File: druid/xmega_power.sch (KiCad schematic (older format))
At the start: 13 parts, among them P8 CONN_01X02, P9 CONN_01X02, U4 XC6206P332MR

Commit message: Design and connect GSM module.
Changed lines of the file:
@@
 Text HLabel 6875 5250 2    60   Output ~ 0
 3.7V
-Text HLabel 5500 4025 0    60   Output ~ 0
-GND
 Connection ~ 5650 4025
 Connection ~ 4500 2250
@@
 	4700 5600 4700 5875
 Connection ~ 4700 5875
+Text GLabel 5500 4025 0    60   Input ~ 0
+GND
 $EndSCHEMATC

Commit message: + new kbd, but not completed + SRAM lines(labels) replaced by bus
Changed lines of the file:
@@
 LIBS:xmega128a1u_bga100
 LIBS:sim-holders
+LIBS:max7370
 LIBS:xmobile-cache
 EELAYER 25 0
@@
 $Descr A4 11693 8268
 encoding utf-8
-Sheet 4 5
+Sheet 3 5
 Title ""
 Date ""
@@
 	1    0    0    -1
 $EndComp
-Text HLabel 8050 2250 2    60   Output ~ 0
-3.3V
-Text HLabel 6875 5250 2    60   Output ~ 0
-3.7V
 Connection ~ 5650 4025
 Connection ~ 4500 2250
@@
 Text GLabel 5500 4025 0    60   Input ~ 0
 GND
+Text GLabel 8050 2250 2    60   Input ~ 0
+3.3V
+Text GLabel 6875 5250 2    60   Input ~ 0
+3.7V
 $EndSCHEMATC

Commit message: SIM cart holder completed. Add micro B slot added
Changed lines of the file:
@@
 F 0 "U4" H 5700 2200 50  0000 C CNN
 F 1 "XC6206P332MR" H 5700 2600 50  0000 C CNN
-F 2 "TO_SOT_Packages_SMD:SOT-23" H 5700 2300 50  0001 C CNN
+F 2 "TO_SOT_Packages_SMD:SOT-23" H 5725 2000 50  0000 C CNN
 F 3 "DOCUMENTATION" H 5700 2300 50  0001 C CNN
 	1    5700 2300

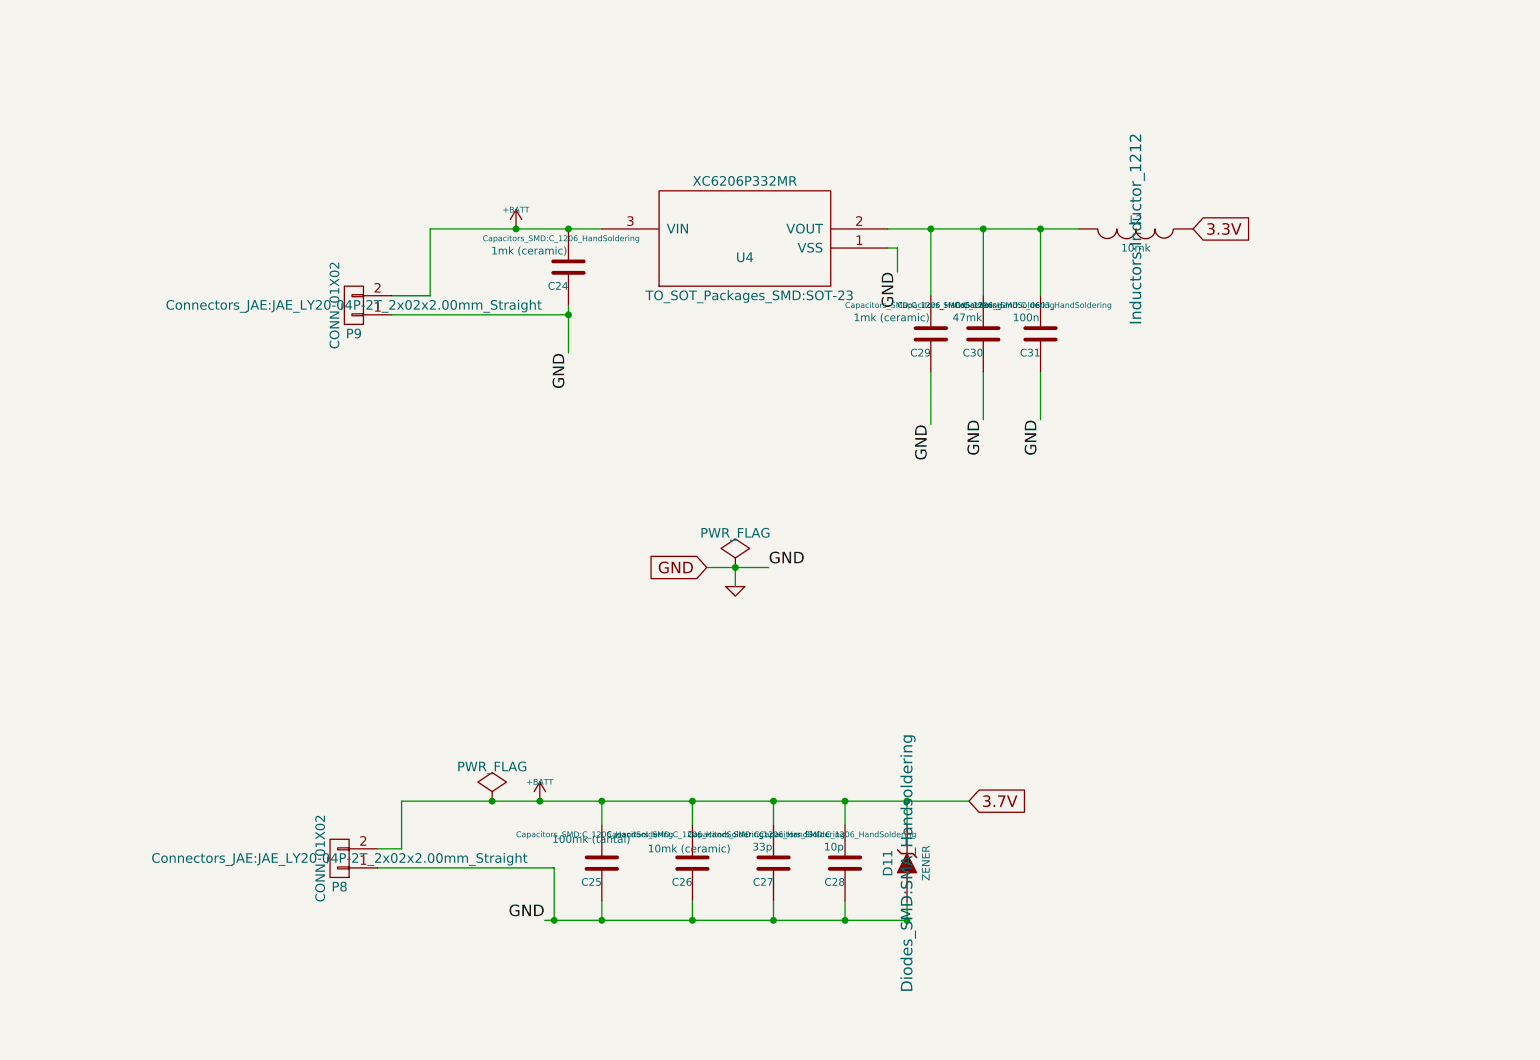
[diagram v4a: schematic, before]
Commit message: Old buttons replaced by membran buttons (electic and pcb) Added pcb for MAX7370 Cleared PCBs of resistor, capacitors and diodes
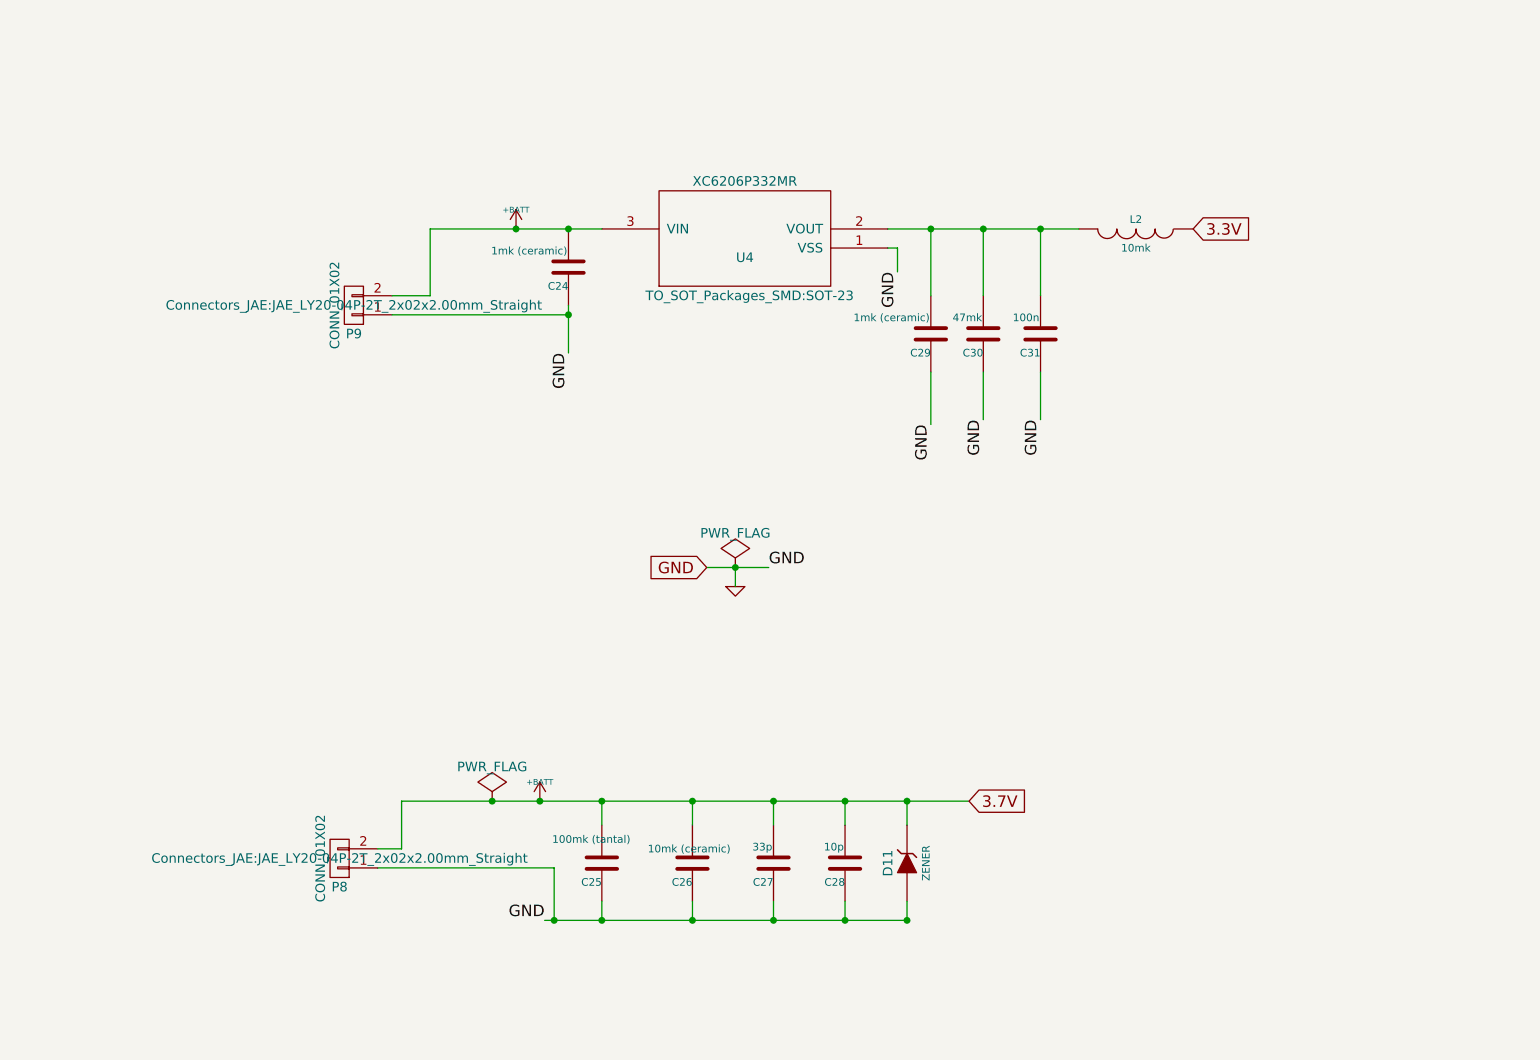
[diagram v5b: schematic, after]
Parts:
- C24, C25, C26, C27, C28, C29, C30: footprint Capacitors_SMD:C_1206_HandSoldering -> (none)
- C31: footprint Capacitors_SMD:C_0603_HandSoldering -> (none)
- D11: footprint Diodes_SMD:SMA_Handsoldering -> (none)
- L2: footprint Inductors:Inductor_1212 -> (none)
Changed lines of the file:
@@
 F 0 "L2" V 7700 2250 40  0000 C CNN
 F 1 "10mk" V 7850 2250 40  0000 C CNN
-F 2 "Inductors:Inductor_1212" H 7750 2250 60  0000 C CNN
+F 2 "" H 7750 2250 60  0000 C CNN
 F 3 "" H 7750 2250 60  0000 C CNN
 	1    7750 2250
@@
 F 0 "C31" H 7250 2900 40  0000 L CNN
 F 1 "100n" H 7256 2715 40  0000 L CNN
-F 2 "Capacitors_SMD:C_0603_HandSoldering" H 7288 2650 30  0000 C CNN
+F 2 "" H 7288 2650 30  0000 C CNN
 F 3 "" H 7250 2800 60  0000 C CNN
 	1    7250 2800
@@
 F 0 "C30" H 6950 2900 40  0000 L CNN
 F 1 "47mk" H 6956 2715 40  0000 L CNN
-F 2 "Capacitors_SMD:C_1206_HandSoldering" H 6988 2650 30  0000 C CNN
+F 2 "" H 6988 2650 30  0000 C CNN
 F 3 "" H 6950 2800 60  0000 C CNN
 	1    6950 2800
@@
 F 0 "C29" H 6675 2900 40  0000 L CNN
 F 1 "1mk (ceramic)" H 6681 2715 40  0000 L CNN
-F 2 "Capacitors_SMD:C_1206_HandSoldering" H 6713 2650 30  0000 C CNN
+F 2 "" H 6713 2650 30  0000 C CNN
 F 3 "" H 6675 2800 60  0000 C CNN
 	1    6675 2800
@@
 F 0 "C24" H 4775 2550 40  0000 L CNN
 F 1 "1mk (ceramic)" H 4781 2365 40  0000 L CNN
-F 2 "Capacitors_SMD:C_1206_HandSoldering" H 4813 2300 30  0000 C CNN
+F 2 "" H 4813 2300 30  0000 C CNN
 F 3 "" H 4775 2450 60  0000 C CNN
 	1    4775 2450
@@
 F 0 "C25" H 4950 5675 40  0000 L CNN
 F 1 "100mk (tantal)" H 4800 5450 40  0000 L CNN
-F 2 "Capacitors_SMD:C_1206_HandSoldering" H 4988 5425 30  0000 C CNN
+F 2 "" H 4988 5425 30  0000 C CNN
 F 3 "" H 4950 5575 60  0000 C CNN
 	1    4950 5575
@@
 F 0 "C26" H 5425 5675 40  0000 L CNN
 F 1 "10mk (ceramic)" H 5225 5500 40  0000 L CNN
-F 2 "Capacitors_SMD:C_1206_HandSoldering" H 5463 5425 30  0000 C CNN
+F 2 "" H 5463 5425 30  0000 C CNN
 F 3 "" H 5425 5575 60  0000 C CNN
 	1    5425 5575
@@
 F 0 "C27" H 5850 5675 40  0000 L CNN
 F 1 "33p" H 5856 5490 40  0000 L CNN
-F 2 "Capacitors_SMD:C_1206_HandSoldering" H 5888 5425 30  0000 C CNN
+F 2 "" H 5888 5425 30  0000 C CNN
 F 3 "" H 5850 5575 60  0000 C CNN
 	1    5850 5575
@@
 F 0 "C28" H 6225 5675 40  0000 L CNN
 F 1 "10p" H 6231 5490 40  0000 L CNN
-F 2 "Capacitors_SMD:C_1206_HandSoldering" H 6263 5425 30  0000 C CNN
+F 2 "" H 6263 5425 30  0000 C CNN
 F 3 "" H 6225 5575 60  0000 C CNN
 	1    6225 5575
@@
 F 0 "D11" H 6550 5675 50  0000 C CNN
 F 1 "ZENER" H 6550 5475 40  0000 C CNN
-F 2 "Diodes_SMD:SMA_Handsoldering" H 6550 5575 60  0000 C CNN
+F 2 "" H 6550 5575 60  0000 C CNN
 F 3 "" H 6550 5575 60  0000 C CNN
 	1    6550 5575

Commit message: Change PDI connector.
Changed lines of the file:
@@
 F 0 "P8" H 3575 5700 50  0000 C CNN
 F 1 "CONN_01X02" V 3675 5550 50  0000 C CNN
-F 2 "Connectors_JAE:JAE_LY20-04P-2T_2x02x2.00mm_Straight" H 3575 5550 50  0000 C CNN
+F 2 "Connectors_JAE:JAE_LY20-04P-2T_2x02x2.00mm_Straight" H 3850 5850 50  0000 C CNN
 F 3 "" H 3575 5550 50  0000 C CNN
 	1    3575 5550

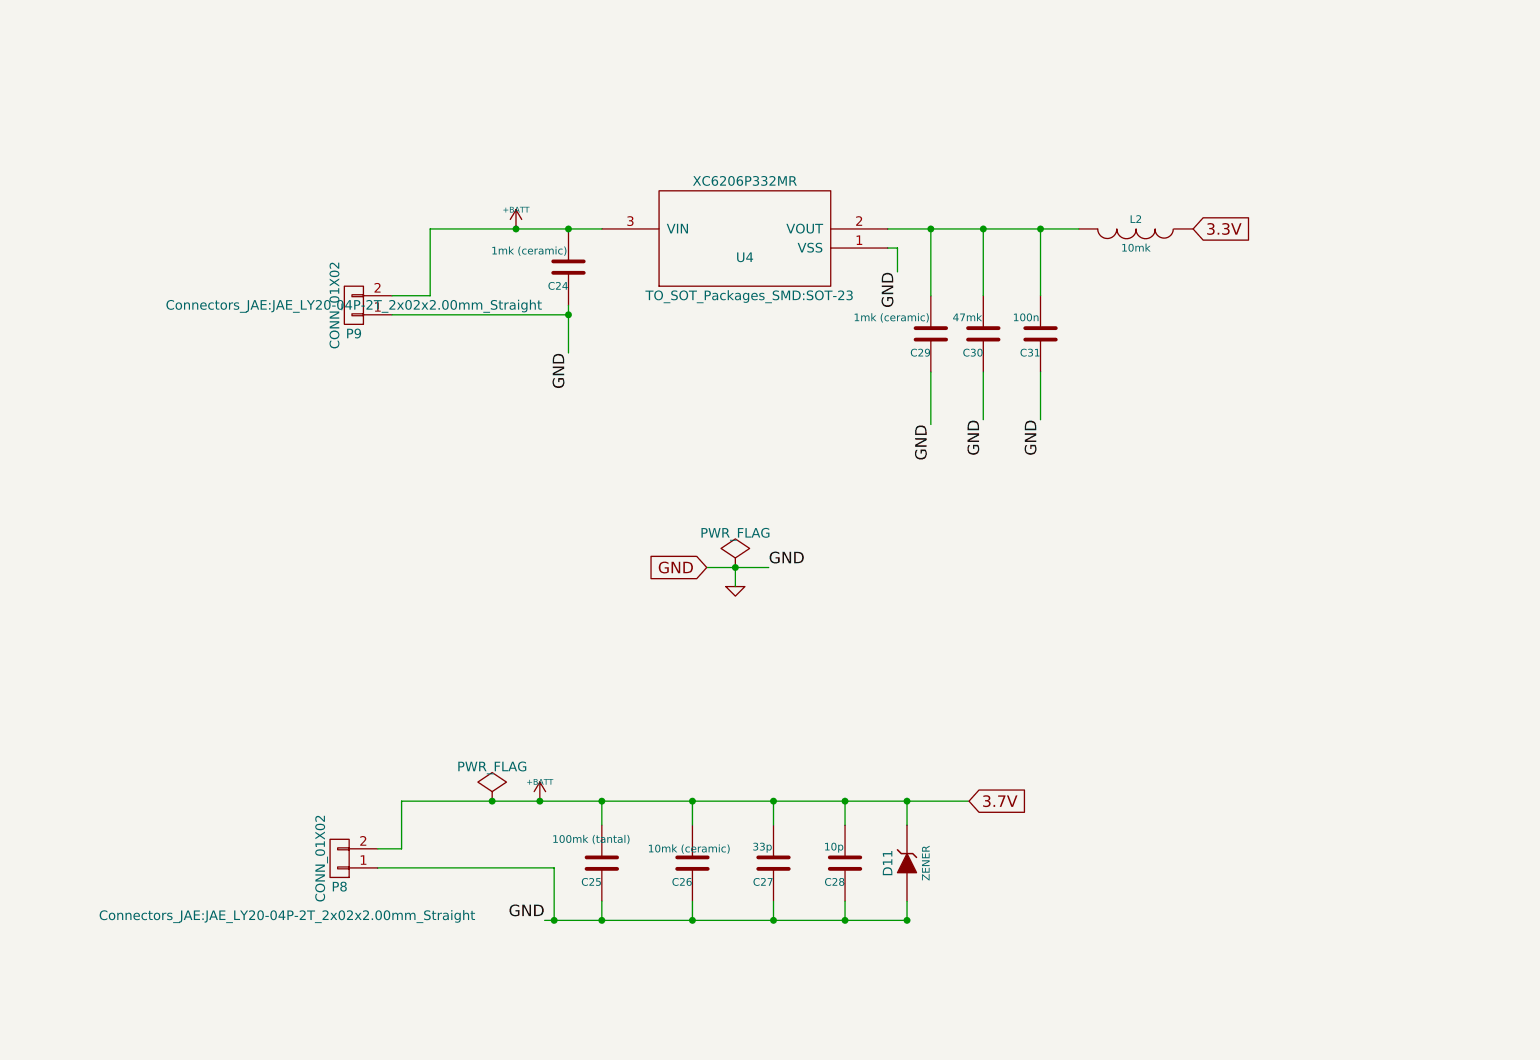
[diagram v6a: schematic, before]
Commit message: Add TP4056 buttary charger (schema and pcb)
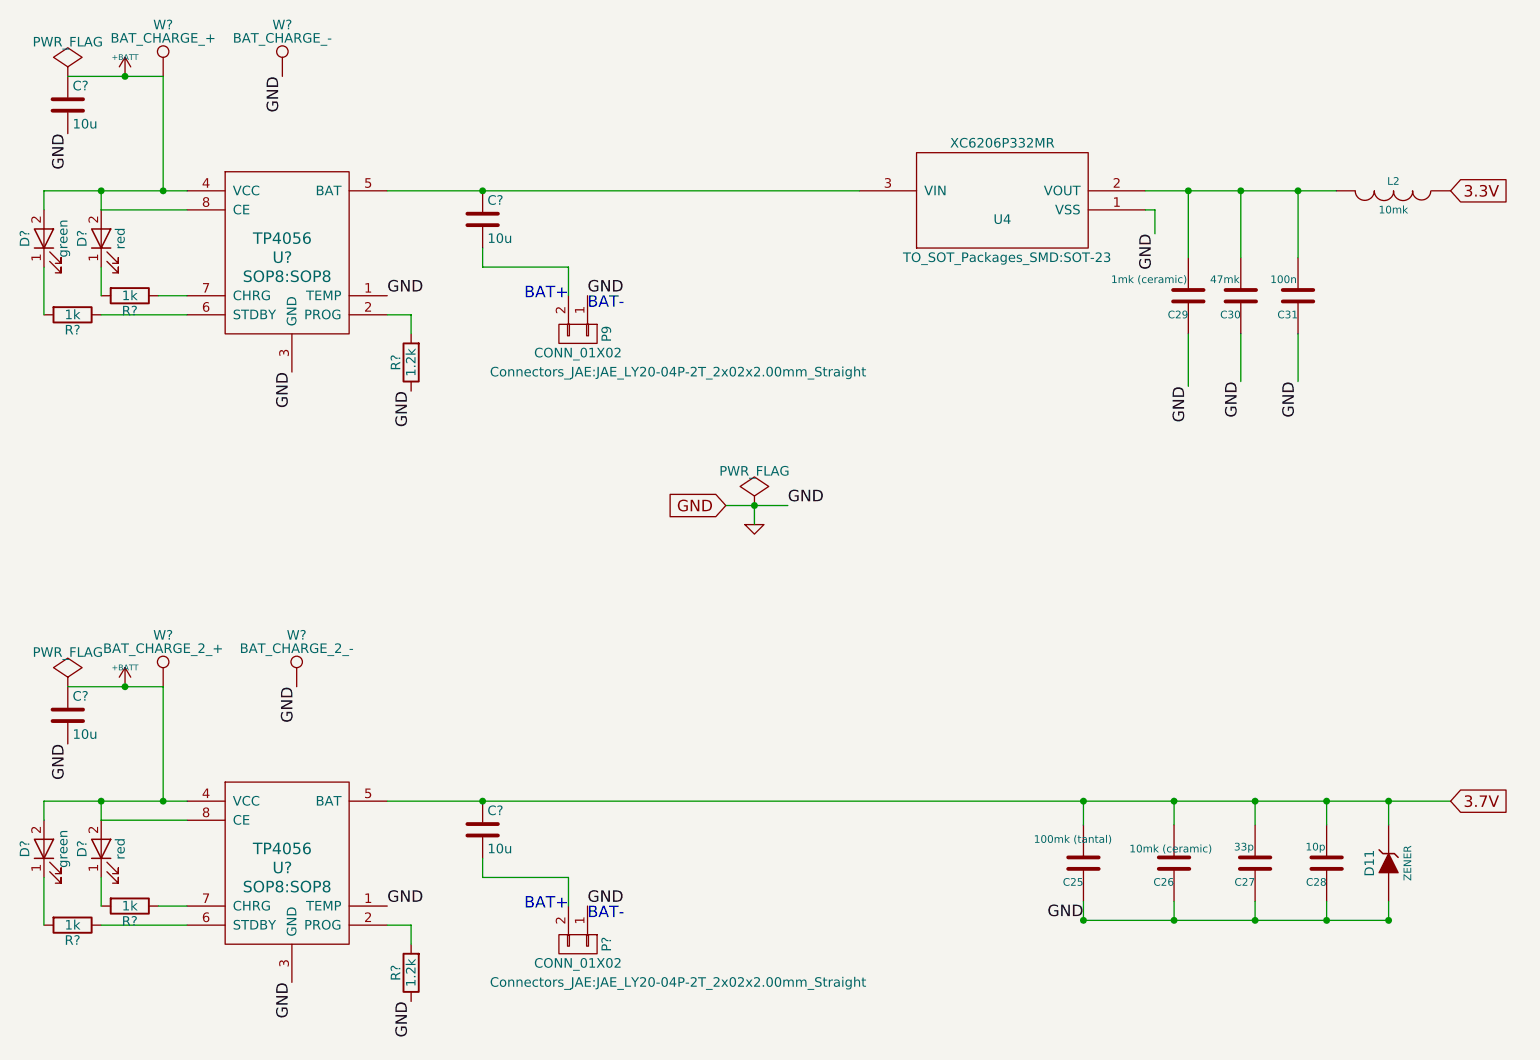
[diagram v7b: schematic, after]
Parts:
- removed C24: 1mk (ceramic), symbol C-RESCUE-xmobile
- removed P8: CONN_01X02, Connectors_JAE:JAE_LY20-04P-2T_2x02x2.00mm_Straight, symbol CONN_01X02
- added C? (x4): 10u, symbol C
- added D? (x2): red, symbol LED-RESCUE-xmobile
- added D? (x2): green, symbol LED-RESCUE-xmobile
- added P?: CONN_01X02, Connectors_JAE:JAE_LY20-04P-2T_2x02x2.00mm_Straight, symbol CONN_01X02
- added R? (x4): 1k, symbol R
- added R? (x2): 1.2k, symbol R
- added U? (x2): TP4056, SOP8:SOP8, symbol TP4056
- added W?: BAT_CHARGE_+, symbol TEST_1P
- added W?: BAT_CHARGE_-, symbol TEST_1P
- added W?: BAT_CHARGE_2_+, symbol TEST_1P
- added W?: BAT_CHARGE_2_-, symbol TEST_1P
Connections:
- net +BATT: now also C?.1, C?.1, D?.2 (A), D?.2 (A), D?.2 (A), D?.2 (A), U?.4 (VCC), U?.4 (VCC), U?.8 (CE), U?.8 (CE), W?.1, W?.1; no longer C25.2, C26.2, C27.2, C28.2, D11.2 (K), P9.2 (P2), U4.3 (VIN)
- net GND: now also C?.2, C?.2, P?.1 (P1), R?.1, R?.1, U?.1 (TEMP), U?.1 (TEMP), U?.3 (GND), U?.3 (GND), W?.1, W?.1
- new net: C?.1, U4.3 (VIN), U?.5 (BAT)
- new net: C?.2, P9.2 (P2)
- new net: R?.2, U?.2 (PROG) (x2)
- new net: R?.1, U?.6 (STDBY) (x2)
- new net: R?.1, U?.7 (CHRG) (x2)
- new net: D?.1 (K), R?.2 (x4)
- new net: C?.2, P?.2 (P2)
- new net 3.7V: C25.2, C26.2, C27.2, C28.2, C?.1, D11.2 (K), U?.5 (BAT)
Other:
- note added: "BAT+\n"
- note added: "BAT-"
- moved on the sheet: C25, C26, C27, C28, C29, C30, C31, D11, L2, P9, U4
